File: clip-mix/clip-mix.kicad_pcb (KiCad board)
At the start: 2 copper layers, 22 parts, among them J1 Conn_01x01_Female, J2 Conn_01x01_Female, J3 Conn_01x01_Female, J4 Conn_02x05_Odd_Even, U1 TL074

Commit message: work on test and clip mix
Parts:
- added REF**: MountingHole_3.2mm_M3, MountingHole:MountingHole_3.2mm_M3, B.Cu at (152.2, 97.3)
- added REF**: MountingHole_3.2mm_M3, MountingHole:MountingHole_3.2mm_M3, B.Cu at (152.3, 135.7)
- C1, C2: value CP1 -> 10uF; moved to B.Cu
- C3, C4: value C -> 0.1uF; moved to B.Cu
- D1, D2: value D -> 1N4148; moved to B.Cu
- D3: value D_Schottky -> 1N5189; moved to B.Cu
- D4: value D_Schottky -> 1N1589; moved to B.Cu
- J1: value Conn_01x01_Female -> IN; moved to B.Cu
- J2: value Conn_01x01_Female -> OUT; moved to B.Cu
- J3: value Conn_01x01_Female -> CLIP OUT; moved to B.Cu
- J4: value Conn_02x05_Odd_Even -> Power; moved to B.Cu
- R1, R2, R3, R4, R7: value R -> 100K; moved to B.Cu
- R5, R8: value R -> 1K; moved to B.Cu
- R6: value R -> 27K; moved to B.Cu
- RV1: value R_POT -> 20K; moved to B.Cu
- U1: moved to B.Cu
- moved C4 56.1 mm to (149.4, 110.0), turned to 0 degrees
- moved D4 55.1 mm to (168.3, 107.0), turned to 180 degrees
- moved J4 53.9 mm to (173.3, 98.1), turned to 90 degrees
- moved C2 53.8 mm to (153.6, 103.8), turned to 180 degrees
- moved U1 53.5 mm to (168.1, 110.8), turned to 180 degrees
- moved C1 53.3 mm to (159.3, 104.0), turned to 180 degrees
- moved D2 52.1 mm to (156.9, 125.3), turned to 180 degrees
- moved C3 51.6 mm to (157.0, 116.0), turned to 180 degrees
- moved R1 51.0 mm to (171.5, 104.5)
- moved R3 49.8 mm to (174.1, 122.1)
- moved R8 49.0 mm to (171.4, 132.0)
- moved J1 48.0 mm to (167.3, 136.3), turned to 180 degrees
- moved D3 47.3 mm to (163.1, 103.5)
- moved RV1 46.3 mm to (161.3, 130.9), turned to 180 degrees
- moved R2 45.6 mm to (174.1, 112.0)
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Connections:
- net Net-(D3-Pad2) renamed +12v
- net Net-(D4-Pad1) renamed -12V
- U1 pad 12: (no net) -> Net-(U1-Pad12)
- U1 pad 13: (no net) -> Net-(U1-Pad12)
- U1 pad 14: (no net) -> Net-(U1-Pad14)
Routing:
- net Earth: track 151.2 -> 111.6 mm
- net Net-(R7-Pad1): track 8.45 -> 34.7 mm
- net Net-(C1-Pad1): track 55.7 -> 33.3 mm
- net Net-(R6-Pad2): track 31.0 -> 17.5 mm
- net Net-(R3-Pad1): track 23.2 -> 10.5 mm
- net Net-(R1-Pad1): track 23.7 -> 11.1 mm
- net Net-(J1-Pad1): track 48.1 -> 39.0 mm
- net Net-(C2-Pad2): track 37.4 -> 28.9 mm
- net Net-(D1-Pad2): track 25.0 -> 30.5 mm
- net -12V: track 9.72 -> 13.5 mm
- net Net-(R2-Pad1): track 17.5 -> 14.0 mm
- net +12v: track 13.5 -> 10.0 mm
- net Net-(D1-Pad1): track 18.3 -> 21.4 mm
- net (no net): track 2.54 -> 0.00 mm
- net Net-(U1-Pad12): track 0.00 -> 2.54 mm
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
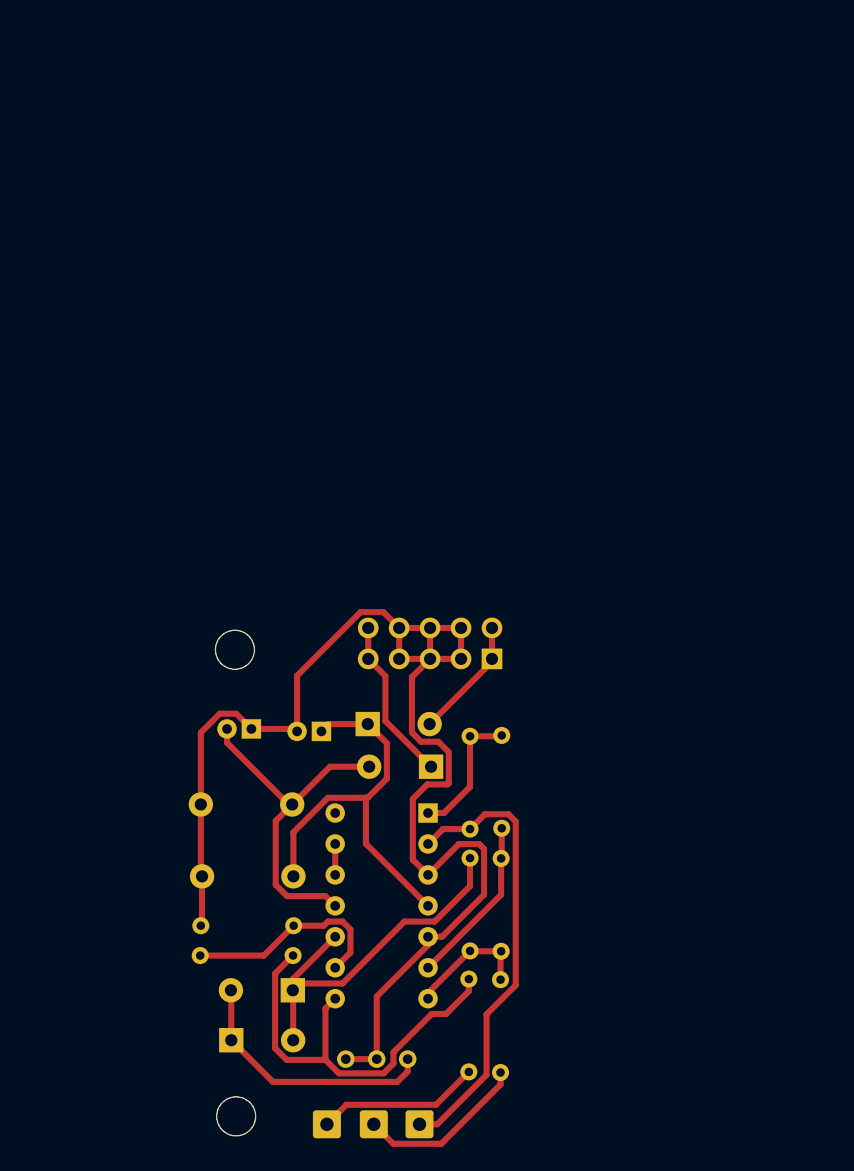
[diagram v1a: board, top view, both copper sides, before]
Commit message: start ASREnvelope
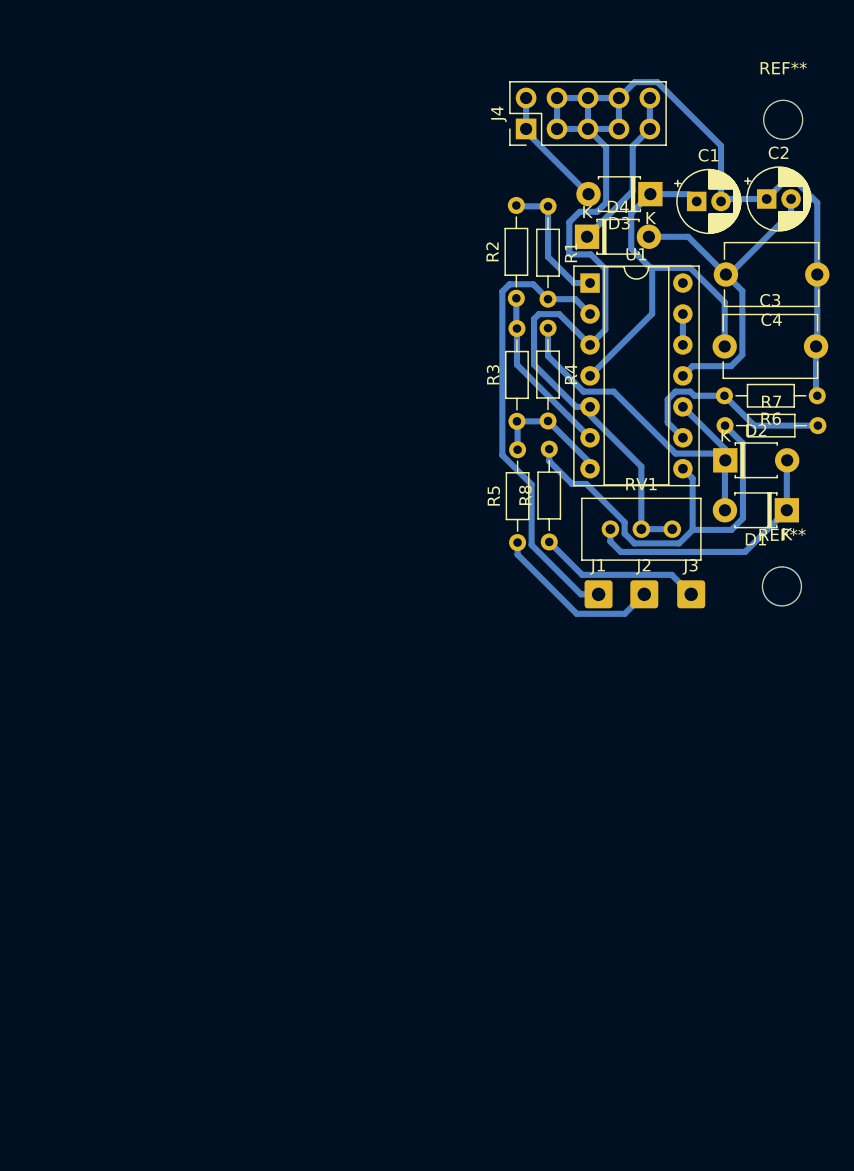
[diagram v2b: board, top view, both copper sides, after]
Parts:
- C1, C2, C3, C4, D1, D2, J1, J2, J3, J4, R1, R2, R3, R4, R5, R6, R7, R8, REF** (x2), RV1, U1: moved to F.Cu
- D3: value 1N5189 -> 1N5819; moved to F.Cu
- D4: value 1N1589 -> 1N5819; moved to F.Cu
- moved C4 66.7 mm to (200.0, 66.5), turned to 180 degrees
- moved R6 66.7 mm to (200.0, 76.5), turned to 180 degrees
- moved D1 63.0 mm to (197.5, 85.9), turned to 180 degrees
- moved REF** 62.6 mm to (197.2, 53.9), turned to 0 degrees
- moved REF** 62.4 mm to (197.1, 92.2), turned to 0 degrees
- moved C2 60.7 mm to (195.8, 60.4), turned to 0 degrees
- moved D2 56.1 mm to (192.4, 81.8), turned to 0 degrees
- moved R7 56.1 mm to (192.4, 79.0), turned to 0 degrees
- moved C3 56.1 mm to (192.4, 72.5), turned to 0 degrees
- moved C1 53.3 mm to (190.1, 60.5), turned to 0 degrees
- moved J3 52.8 mm to (189.7, 92.8), turned to 0 degrees
- moved RV1 51.1 mm to (188.1, 87.5), turned to 0 degrees
- moved D3 49.3 mm to (186.3, 60.0), turned to 180 degrees
- moved J2 48.8 mm to (185.8, 92.8), turned to 0 degrees
- moved J1 45.9 mm to (182.1, 92.8), turned to 0 degrees
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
